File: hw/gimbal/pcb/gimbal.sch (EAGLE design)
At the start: 75 parts, among them J1 JST-XH4SMT_RA, U1 STM32F4R_64PIN, U2 TPS62172PWSON8, U3 TPS55330PQFN16, U4 MC33926, U5 DRV8313, U6 DRV8313, U7 AS5048A

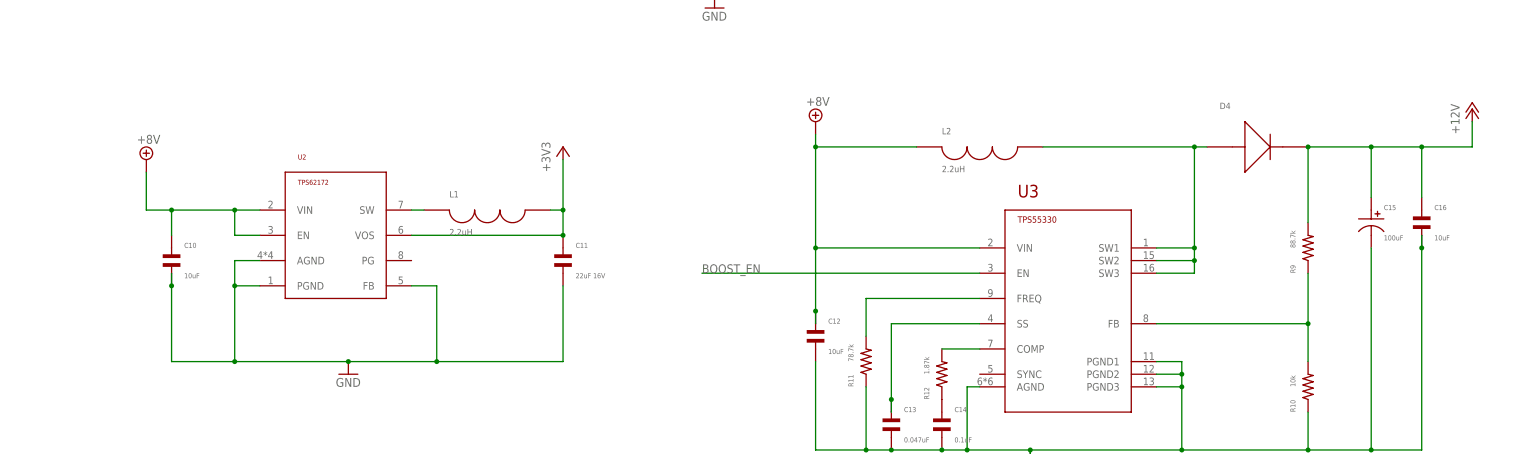
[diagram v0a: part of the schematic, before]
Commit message: gimbal board: Add test points for power rail, and an overall board label on the silk layer.
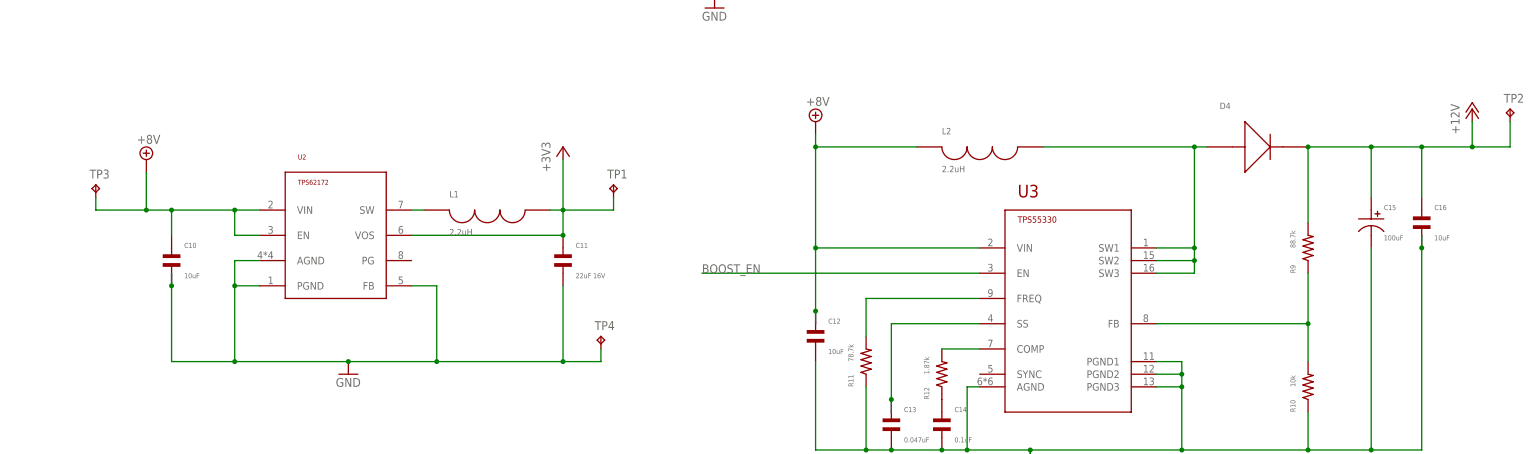
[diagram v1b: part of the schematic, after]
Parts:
- added TP1, TP2, TP3, TP4: TPPAD1-13, testpad:TPPAD1-13
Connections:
- net +12V: now also TP2.TP
- net +3V3: now also TP1.TP
- net +8V: now also TP3.TP
- net GND: now also TP4.TP
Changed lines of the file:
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@@
 </part>
 <part name="PABS" library="gimbal" deviceset="JST-ZH4" device="">
-<attribute name="DPN" value="455-1683-1-ND	"/>
+<attribute name="DPN" value="455-1683-1-ND "/>
 </part>
 <part name="PIMU" library="gimbal" deviceset="JST-ZH4" device="">
@@
 <attribute name="AMFPN" value="MF-RES-0603-1.69K"/>
 </part>
+<part name="TP1" library="testpad" deviceset="TP" device="PAD1-13"/>
+<part name="TP2" library="testpad" deviceset="TP" device="PAD1-13"/>
+<part name="TP3" library="testpad" deviceset="TP" device="PAD1-13"/>
+<part name="TP4" library="testpad" deviceset="TP" device="PAD1-13"/>
 </parts>
 <sheets>
@@
 <attribute name="AMFPN" x="35.56" y="-312.42" size="1.778" layer="96" rot="R90" display="off"/>
 </instance>
+<instance part="TP1" gate="G$1" x="83.82" y="71.12"/>
+<instance part="TP2" gate="G$1" x="264.16" y="86.36"/>
+<instance part="TP3" gate="G$1" x="-20.32" y="71.12"/>
+<instance part="TP4" gate="G$1" x="81.28" y="40.64"/>
 </instances>
 <busses>
@@
 <pinref part="C11" gate="G$1" pin="P$2"/>
 <wire x1="73.66" y1="35.56" x2="73.66" y2="50.8" width="0.1524" layer="91"/>
+<pinref part="TP4" gate="G$1" pin="TP"/>
+<wire x1="73.66" y1="35.56" x2="81.28" y2="35.56" width="0.1524" layer="91"/>
+<wire x1="81.28" y1="35.56" x2="81.28" y2="38.1" width="0.1524" layer="91"/>
+<junction x="73.66" y="35.56"/>
 </segment>
 <segment>
@@
 <pinref part="C11" gate="G$1" pin="P$1"/>
 <junction x="73.66" y="60.96"/>
+<pinref part="TP1" gate="G$1" pin="TP"/>
+<wire x1="73.66" y1="66.04" x2="83.82" y2="66.04" width="0.1524" layer="91"/>
+<wire x1="83.82" y1="66.04" x2="83.82" y2="68.58" width="0.1524" layer="91"/>
 </segment>
 <segment>
@@
 <junction x="-5.08" y="66.04"/>
 <pinref part="C10" gate="G$1" pin="P$1"/>
+<pinref part="TP3" gate="G$1" pin="TP"/>
+<wire x1="-20.32" y1="68.58" x2="-20.32" y2="66.04" width="0.1524" layer="91"/>
+<wire x1="-20.32" y1="66.04" x2="-10.16" y2="66.04" width="0.1524" layer="91"/>
+<junction x="-10.16" y="66.04"/>
 </segment>
 <segment>
@@
 <junction x="223.52" y="78.74"/>
 <pinref part="C16" gate="G$1" pin="P$1"/>
-</segment>
-<segment>
+<pinref part="TP2" gate="G$1" pin="TP"/>
+<wire x1="256.54" y1="78.74" x2="264.16" y2="78.74" width="0.1524" layer="91"/>
+<wire x1="264.16" y1="78.74" x2="264.16" y2="83.82" width="0.1524" layer="91"/>
+<junction x="256.54" y="78.74"/>
+</segment>
+<segment>

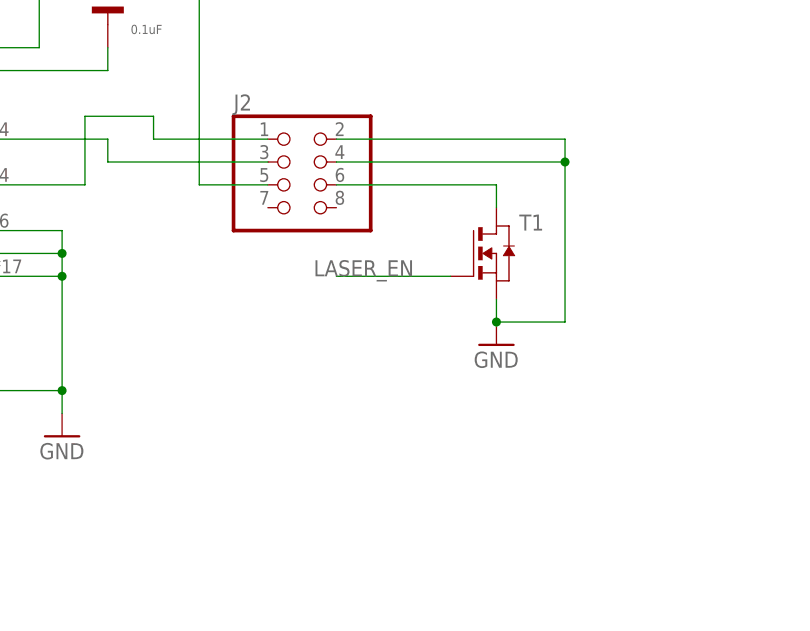
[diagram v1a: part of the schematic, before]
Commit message: gimbal board: Audited all package footprints and part values.  Fixed inconsistencies.
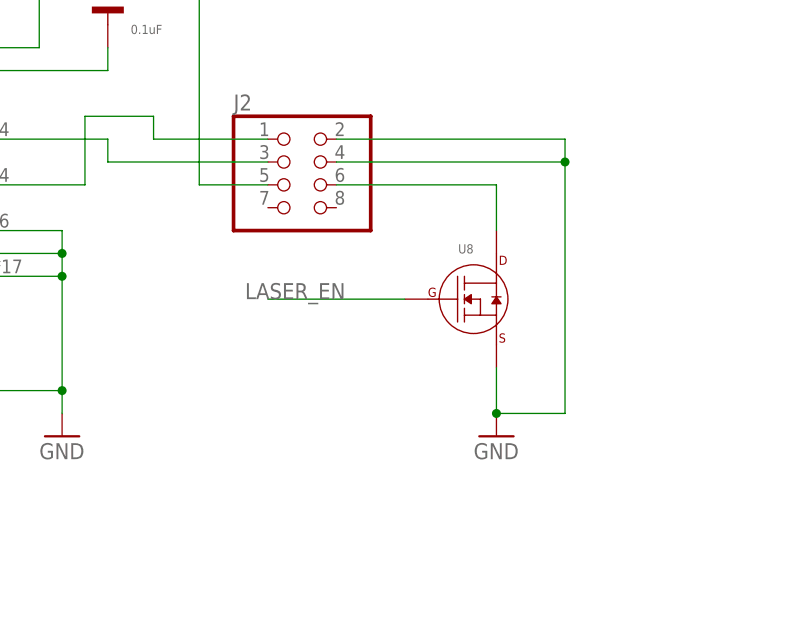
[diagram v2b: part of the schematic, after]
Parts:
- removed T1: (no value), zetex:NMOSSOT23
- added U8: (no value), mfdiscrete:N-CHANNEL_FET_SOT-23-3
- ARM: DPN 401-2002-6-ND -> 401-2002-1-ND
- Q1: device gimbal:CRYSTALSMD5X3.2 -> gimbal:CRYSTALABM3B
- R13: DPN P88.7KHDKR-ND -> P100KHCT-ND
- R14: DPN P220HDKR-ND -> P220HCT-ND
- R9: DPN P88.7KHDKR-ND -> P88.7KHCT-ND
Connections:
- net GND: now also U8.SOURCE; no longer T1.S
- net LASER_EN: now also U8.GATE; no longer T1.G
- net N$1: now also U8.DRAIN; no longer T1.D
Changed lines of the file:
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@@
 <part name="MOUNT1" library="gimbal" deviceset="M3_MOTOR_MOUNT" device=""/>
 <part name="MOUNT2" library="gimbal" deviceset="M3_MOTOR_MOUNT" device=""/>
-<part name="T1" library="zetex" deviceset="NMOSSOT23" device="">
-<attribute name="AMFPN" value="MF-DSC-SOT233-BSS84"/>
-</part>
 <part name="GND1" library="supply1" deviceset="GND" device=""/>
 <part name="GND2" library="supply1" deviceset="GND" device=""/>
 <part name="+3V1" library="supply1" deviceset="+3V3" device=""/>
 <part name="R13" library="mfpassives" deviceset="RESISTOR" device="_0603" value="100k">
-<attribute name="DPN" value="P88.7KHDKR-ND"/>
+<attribute name="DPN" value="P100KHCT-ND"/>
 </part>
 <part name="R14" library="mfpassives" deviceset="RESISTOR" device="_0603" value="220">
-<attribute name="DPN" value="P220HDKR-ND"/>
+<attribute name="DPN" value="P220HCT-ND"/>
 </part>
 <part name="SUPPLY1" library="supply2" deviceset="+8V" device=""/>
@@
 </part>
 <part name="R9" library="mfpassives" deviceset="RESISTOR" device="_0603" value="88.7k">
-<attribute name="DPN" value="P88.7KHDKR-ND"/>
+<attribute name="DPN" value="P88.7KHCT-ND"/>
 </part>
 <part name="R10" library="mfpassives" deviceset="RESISTOR" device="_0603" value="10k">
@@
 <attribute name="AMFPN" value="MF-RES-0603-10"/>
 </part>
-<part name="Q1" library="gimbal" deviceset="CRYSTAL" device="SMD5X3.2">
+<part name="Q1" library="gimbal" deviceset="CRYSTAL" device="ABM3B">
 <attribute name="DPN" value="535-9721-1-ND"/>
 </part>
@@
 </part>
 <part name="ARM" library="gimbal" deviceset="SLIDE_SWITCH" device="JS_SUB_SWITCH">
-<attribute name="DPN" value="401-2002-6-ND"/>
+<attribute name="DPN" value="401-2002-1-ND"/>
 </part>
 <part name="GND19" library="supply1" deviceset="GND" device=""/>
@@
 <part name="TP3" library="testpad" deviceset="TP" device="PAD1-13"/>
 <part name="TP4" library="testpad" deviceset="TP" device="PAD1-13"/>
+<part name="U8" library="mfdiscrete" deviceset="N-CHANNEL_FET" device="_SOT-23-3"/>
 </parts>
 <sheets>
@@
 <instance part="MOUNT1" gate="G$1" x="-22.86" y="-383.54"/>
 <instance part="MOUNT2" gate="G$1" x="-22.86" y="-398.78"/>
-<instance part="T1" gate="A" x="205.74" y="-58.42">
-<attribute name="AMFPN" x="205.74" y="-58.42" size="1.778" layer="96" display="off"/>
-</instance>
-<instance part="GND1" gate="1" x="205.74" y="-68.58"/>
+<instance part="GND1" gate="1" x="205.74" y="-78.74"/>
 <instance part="GND2" gate="1" x="157.48" y="-78.74"/>
 <instance part="+3V1" gate="G$1" x="96.52" y="0"/>
@@
 <instance part="TP3" gate="G$1" x="-20.32" y="71.12"/>
 <instance part="TP4" gate="G$1" x="81.28" y="40.64"/>
+<instance part="U8" gate="G$1" x="203.2" y="-63.5"/>
 </instances>
 <busses>
@@
 <segment>
 <pinref part="J2" gate="A" pin="6"/>
-<pinref part="T1" gate="A" pin="D"/>
 <wire x1="187.96" y1="-50.8" x2="205.74" y2="-50.8" width="0.1524" layer="91"/>
-<wire x1="205.74" y1="-50.8" x2="205.74" y2="-53.34" width="0.1524" layer="91"/>
+<pinref part="U8" gate="G$1" pin="DRAIN"/>
+<wire x1="205.74" y1="-55.88" x2="205.74" y2="-50.8" width="0.1524" layer="91"/>
 </segment>
 </net>
 <net name="GND" class="0">
 <segment>
-<pinref part="T1" gate="A" pin="S"/>
 <pinref part="GND1" gate="1" pin="GND"/>
-<wire x1="205.74" y1="-63.5" x2="205.74" y2="-66.04" width="0.1524" layer="91"/>
-<wire x1="205.74" y1="-66.04" x2="213.36" y2="-66.04" width="0.1524" layer="91"/>
-<wire x1="213.36" y1="-66.04" x2="213.36" y2="-48.26" width="0.1524" layer="91"/>
-<junction x="205.74" y="-66.04"/>
+<wire x1="205.74" y1="-76.2" x2="213.36" y2="-76.2" width="0.1524" layer="91"/>
+<wire x1="213.36" y1="-76.2" x2="213.36" y2="-48.26" width="0.1524" layer="91"/>
+<junction x="205.74" y="-76.2"/>
 <pinref part="J2" gate="A" pin="4"/>
 <wire x1="213.36" y1="-48.26" x2="187.96" y2="-48.26" width="0.1524" layer="91"/>
@@
 <wire x1="213.36" y1="-45.72" x2="213.36" y2="-48.26" width="0.1524" layer="91"/>
 <junction x="213.36" y="-48.26"/>
+<pinref part="U8" gate="G$1" pin="SOURCE"/>
+<wire x1="205.74" y1="-71.12" x2="205.74" y2="-76.2" width="0.1524" layer="91"/>
 </segment>
 <segment>
@@
 <net name="LASER_EN" class="0">
 <segment>
-<pinref part="T1" gate="A" pin="G"/>
-<wire x1="200.66" y1="-60.96" x2="187.96" y2="-60.96" width="0.1524" layer="91"/>
-<label x="185.42" y="-60.96" size="1.778" layer="95"/>
-</segment>
-<segment>
+<wire x1="195.58" y1="-63.5" x2="180.34" y2="-63.5" width="0.1524" layer="91"/>
+<label x="177.8" y="-63.5" size="1.778" layer="95"/>
+<pinref part="U8" gate="G$1" pin="GATE"/>
+</segment>
+<segment>
